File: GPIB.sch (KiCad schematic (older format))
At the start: 11 parts

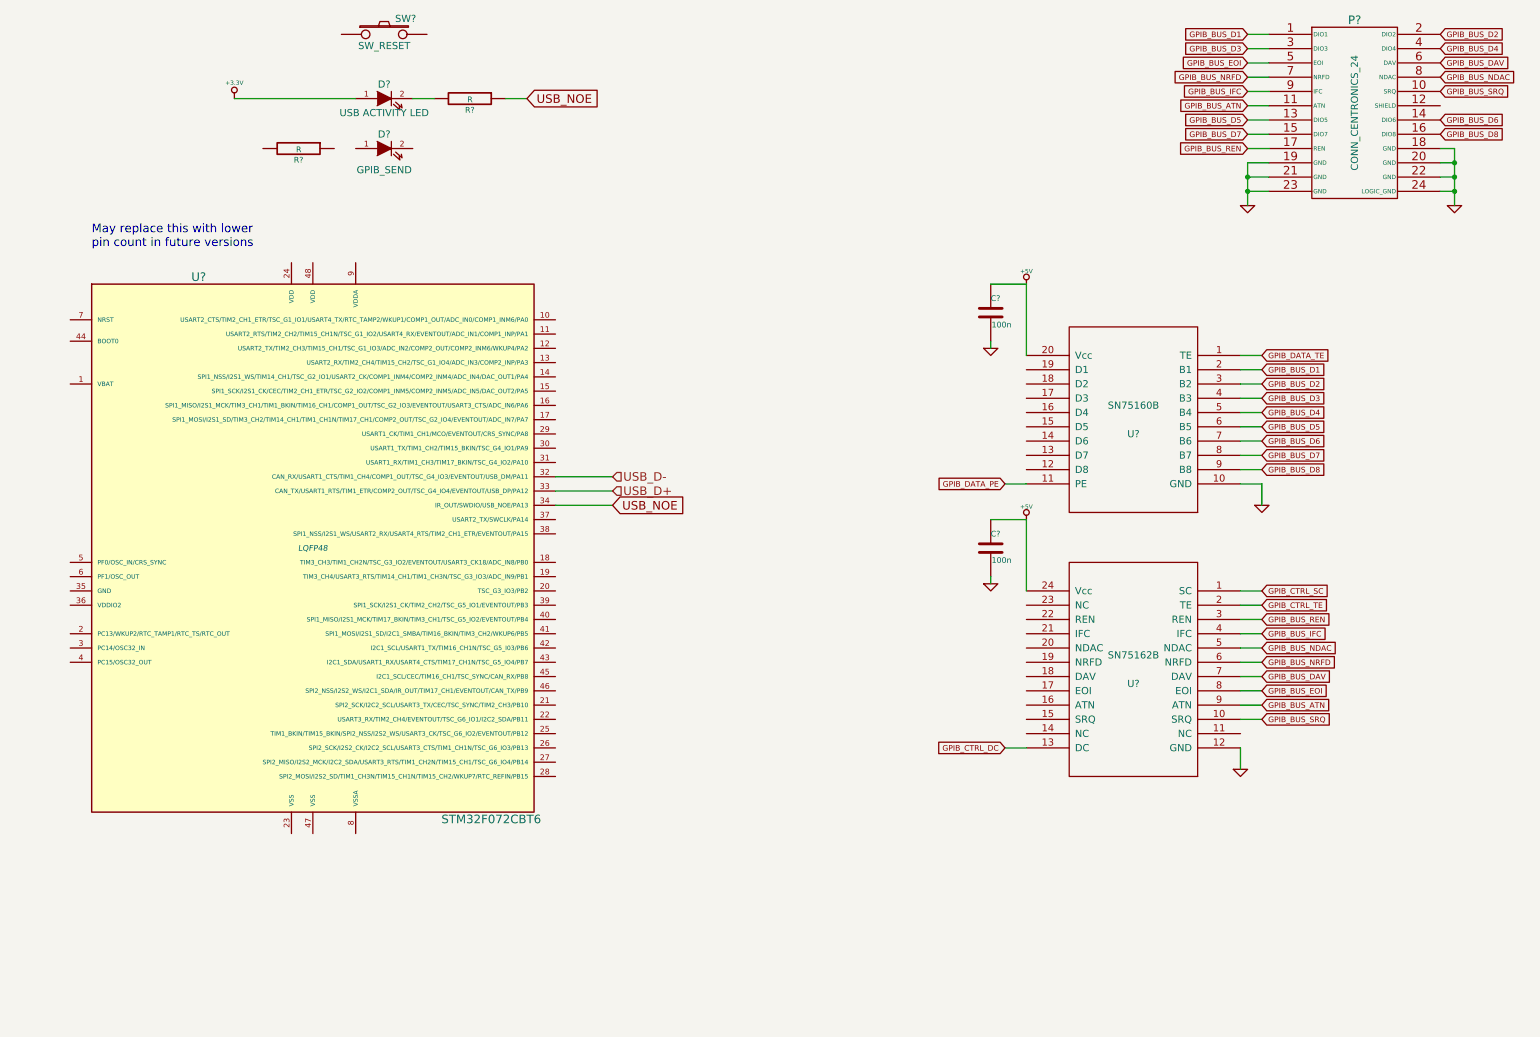
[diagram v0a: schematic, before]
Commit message: Add reset circuit
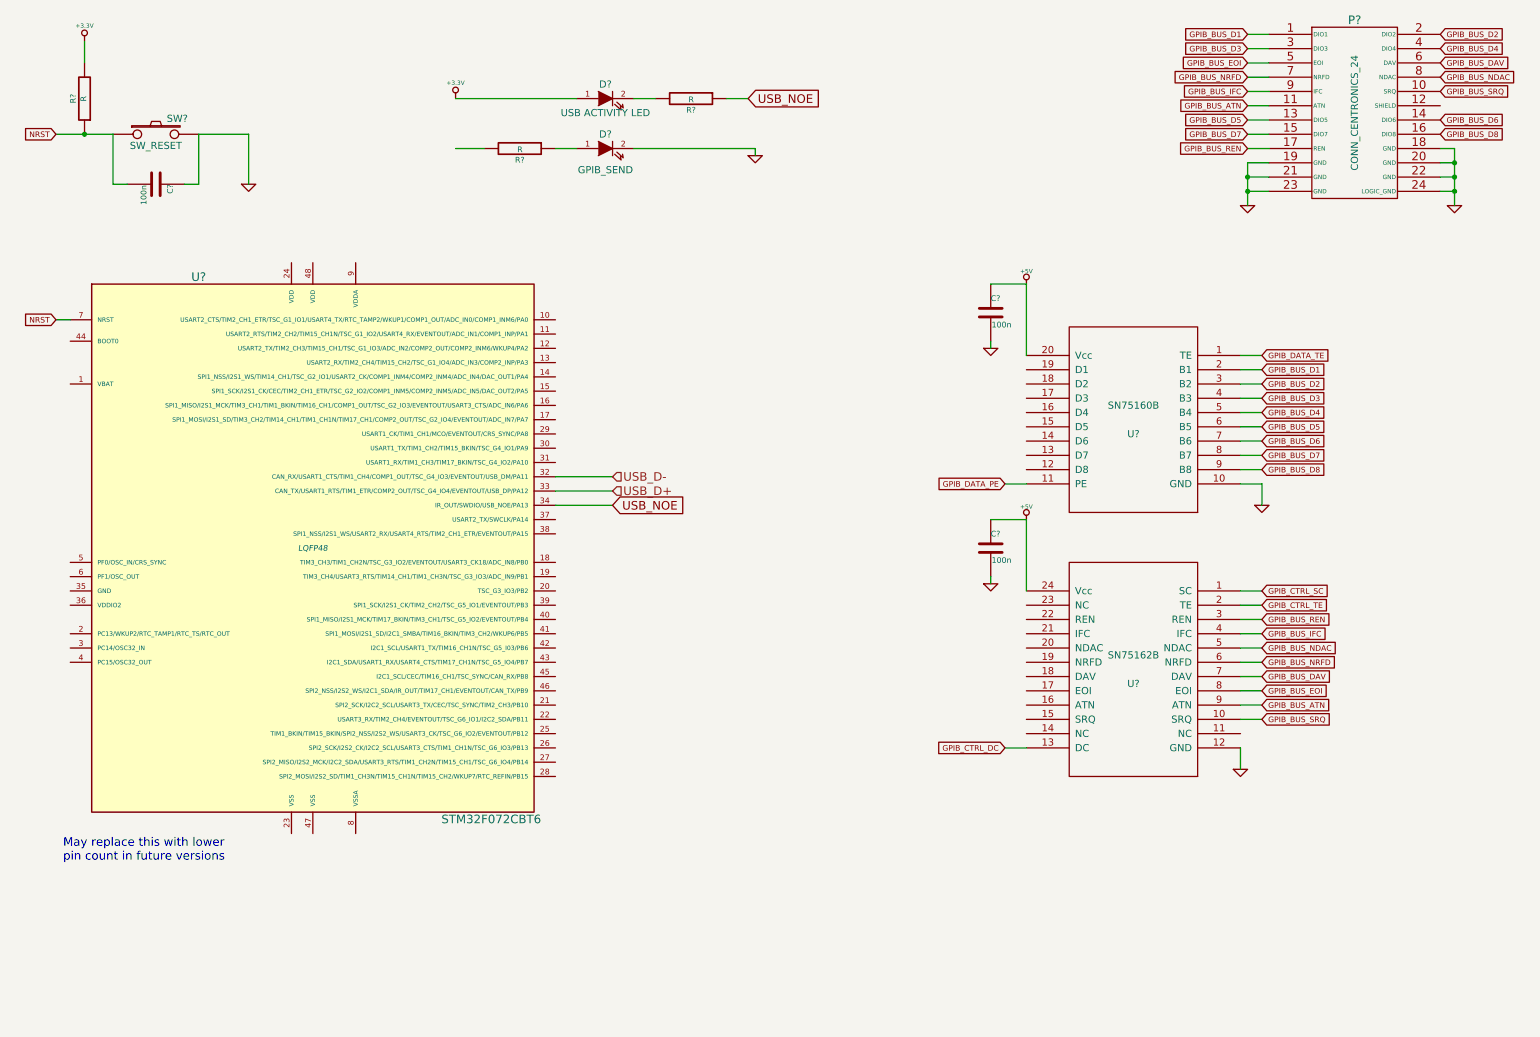
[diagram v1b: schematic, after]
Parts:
- added C?: 100n, symbol C
- added R?: R, symbol R
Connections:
- net +3.3V: now also R?.2
- net GND: now also D?.2 (K), SW?.2, C?.1
- net NRST: now reaches SW?.1
- net NRST: now also U?.7 (NRST), C?.2, R?.1
- net at D?.1 (A): now also R?.1
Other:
- moved on the sheet: D?, R?, SW?
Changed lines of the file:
@@
 L SW_PUSH SW?
 U 1 1 5566861E
-P 3250 750
-F 0 "SW?" H 3400 860 50  0000 C CNN
-F 1 "SW_RESET" H 3250 670 50  0000 C CNN
-F 2 "" H 3250 750 60  0000 C CNN
-F 3 "" H 3250 750 60  0000 C CNN
-	1    3250 750
+P 1650 1450
+F 0 "SW?" H 1800 1560 50  0000 C CNN
+F 1 "SW_RESET" H 1650 1370 50  0000 C CNN
+F 2 "" H 1650 1450 60  0000 C CNN
+F 3 "" H 1650 1450 60  0000 C CNN
+	1    1650 1450
 	1    0    0    -1
 $EndComp
@@
 L LED D?
 U 1 1 55668641
-P 3250 1550
-F 0 "D?" H 3250 1650 50  0000 C CNN
-F 1 "GPIB_SEND" H 3250 1400 50  0000 C CNN
-F 2 "" H 3250 1550 60  0000 C CNN
-F 3 "" H 3250 1550 60  0000 C CNN
-	1    3250 1550
-	1    0    0    -1
-$EndComp
-Text Notes 1200 2250 0    60   ~ 0
+P 4800 1550
+F 0 "D?" H 4800 1650 50  0000 C CNN
+F 1 "GPIB_SEND" H 4800 1400 50  0000 C CNN
+F 2 "" H 4800 1550 60  0000 C CNN
+F 3 "" H 4800 1550 60  0000 C CNN
+	1    4800 1550
+	1    0    0    -1
+$EndComp
+Text Notes 1000 6550 0    60   ~ 0
 May replace this with lower\npin count in future versions
 $Comp
@@
 L LED D?
 U 1 1 5567B154
-P 3250 1200
-F 0 "D?" H 3250 1300 50  0000 C CNN
-F 1 "USB ACTIVITY LED" H 3250 1100 50  0000 C CNN
-F 2 "" H 3250 1200 60  0000 C CNN
-F 3 "" H 3250 1200 60  0000 C CNN
-	1    3250 1200
+P 4800 1200
+F 0 "D?" H 4800 1300 50  0000 C CNN
+F 1 "USB ACTIVITY LED" H 4800 1100 50  0000 C CNN
+F 2 "" H 4800 1200 60  0000 C CNN
+F 3 "" H 4800 1200 60  0000 C CNN
+	1    4800 1200
 	1    0    0    -1
 $EndComp
@@
 L +3.3V #PWR?
 U 1 1 5567B18B
-P 2200 1200
-F 0 "#PWR?" H 2200 1160 30  0001 C CNN
-F 1 "+3.3V" H 2200 1310 30  0000 C CNN
-F 2 "" H 2200 1200 60  0000 C CNN
-F 3 "" H 2200 1200 60  0000 C CNN
-	1    2200 1200
-	1    0    0    -1
-$EndComp
-Wire Wire Line
-	2200 1200 3050 1200
+P 3750 1200
+F 0 "#PWR?" H 3750 1160 30  0001 C CNN
+F 1 "+3.3V" H 3750 1310 30  0000 C CNN
+F 2 "" H 3750 1200 60  0000 C CNN
+F 3 "" H 3750 1200 60  0000 C CNN
+	1    3750 1200
+	1    0    0    -1
+$EndComp
+Wire Wire Line
+	3750 1200 4600 1200
 $Comp
 L R R?
 U 1 1 5567B1D4
-P 3850 1200
-F 0 "R?" V 3930 1200 40  0000 C CNN
-F 1 "R" V 3857 1201 40  0000 C CNN
-F 2 "" V 3780 1200 30  0000 C CNN
-F 3 "" H 3850 1200 30  0000 C CNN
-	1    3850 1200
+P 5400 1200
+F 0 "R?" V 5480 1200 40  0000 C CNN
+F 1 "R" V 5407 1201 40  0000 C CNN
+F 2 "" V 5330 1200 30  0000 C CNN
+F 3 "" H 5400 1200 30  0000 C CNN
+	1    5400 1200
 	0    1    1    0
 $EndComp
 Wire Wire Line
-	3450 1200 3600 1200
-Wire Wire Line
-	4100 1200 4250 1200
+	5000 1200 5150 1200
+Wire Wire Line
+	5650 1200 5800 1200
 Text GLabel 4850 4050 2    60   Input ~ 0
 USB_NOE
-Text GLabel 4250 1200 2    60   Input ~ 0
+Text GLabel 5800 1200 2    60   Input ~ 0
 USB_NOE
 $Comp
 L R R?
 U 1 1 5567BB74
-P 2650 1550
-F 0 "R?" V 2730 1550 40  0000 C CNN
-F 1 "R" V 2657 1551 40  0000 C CNN
-F 2 "" V 2580 1550 30  0000 C CNN
-F 3 "" H 2650 1550 30  0000 C CNN
-	1    2650 1550
+P 4200 1550
+F 0 "R?" V 4280 1550 40  0000 C CNN
+F 1 "R" V 4207 1551 40  0000 C CNN
+F 2 "" V 4130 1550 30  0000 C CNN
+F 3 "" H 4200 1550 30  0000 C CNN
+	1    4200 1550
 	0    1    1    0
 $EndComp
@@
 Wire Wire Line
 	7500 4150 7750 4150
+$Comp
+L GND #PWR?
+U 1 1 5569A4CE
+P 5850 1600
+F 0 "#PWR?" H 5850 1600 30  0001 C CNN
+F 1 "GND" H 5850 1530 30  0001 C CNN
+F 2 "" H 5850 1600 60  0000 C CNN
+F 3 "" H 5850 1600 60  0000 C CNN
+	1    5850 1600
+	1    0    0    -1
+$EndComp
+Wire Wire Line
+	5000 1550 5850 1550
+Wire Wire Line
+	5850 1550 5850 1600
+Wire Wire Line
+	4600 1550 4450 1550
+Wire Wire Line
+	3950 1550 3750 1550
+$Comp
+L +3.3V #PWR?
+U 1 1 5569A6B6
+P 1150 800
+F 0 "#PWR?" H 1150 760 30  0001 C CNN
+F 1 "+3.3V" H 1150 910 30  0000 C CNN
+F 2 "" H 1150 800 60  0000 C CNN
+F 3 "" H 1150 800 60  0000 C CNN
+	1    1150 800
+	1    0    0    -1
+$EndComp
+$Comp
+L GND #PWR?
+U 1 1 5569A6D7
+P 2300 1800
+F 0 "#PWR?" H 2300 1800 30  0001 C CNN
+F 1 "GND" H 2300 1730 30  0001 C CNN
+F 2 "" H 2300 1800 60  0000 C CNN
+F 3 "" H 2300 1800 60  0000 C CNN
+	1    2300 1800
+	1    0    0    -1
+$EndComp
+$Comp
+L C C?
+U 1 1 5569A6F8
+P 1650 1800
+F 0 "C?" H 1650 1900 40  0000 L CNN
+F 1 "100n" H 1656 1715 40  0000 L CNN
+F 2 "" H 1688 1650 30  0000 C CNN
+F 3 "" H 1650 1800 60  0000 C CNN
+	1    1650 1800
+	0    1    1    0
+$EndComp
+$Comp
+L R R?
+U 1 1 5569A770
+P 1150 1200
+F 0 "R?" V 1230 1200 40  0000 C CNN
+F 1 "R" V 1157 1201 40  0000 C CNN
+F 2 "" V 1080 1200 30  0000 C CNN
+F 3 "" H 1150 1200 30  0000 C CNN
+	1    1150 1200
+	-1   0    0    1
+$EndComp
+Wire Wire Line
+	1150 800  1150 950
+Wire Wire Line
+	950  1450 1350 1450
+Connection ~ 1150 1450
+Wire Wire Line
+	1350 1450 1350 1800
+Wire Wire Line
+	1350 1800 1450 1800
+Wire Wire Line
+	1950 1450 1950 1800
+Wire Wire Line
+	1950 1800 1850 1800
+Wire Wire Line
+	1950 1450 2300 1450
+Wire Wire Line
+	2300 1450 2300 1800
+Wire Wire Line
+	1050 2750 950  2750
+Text GLabel 950  2750 0    39   Input ~ 0
+NRST
+Text GLabel 950  1450 0    39   Input ~ 0
+NRST
 $EndSCHEMATC

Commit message: initial GPIB pin mappings
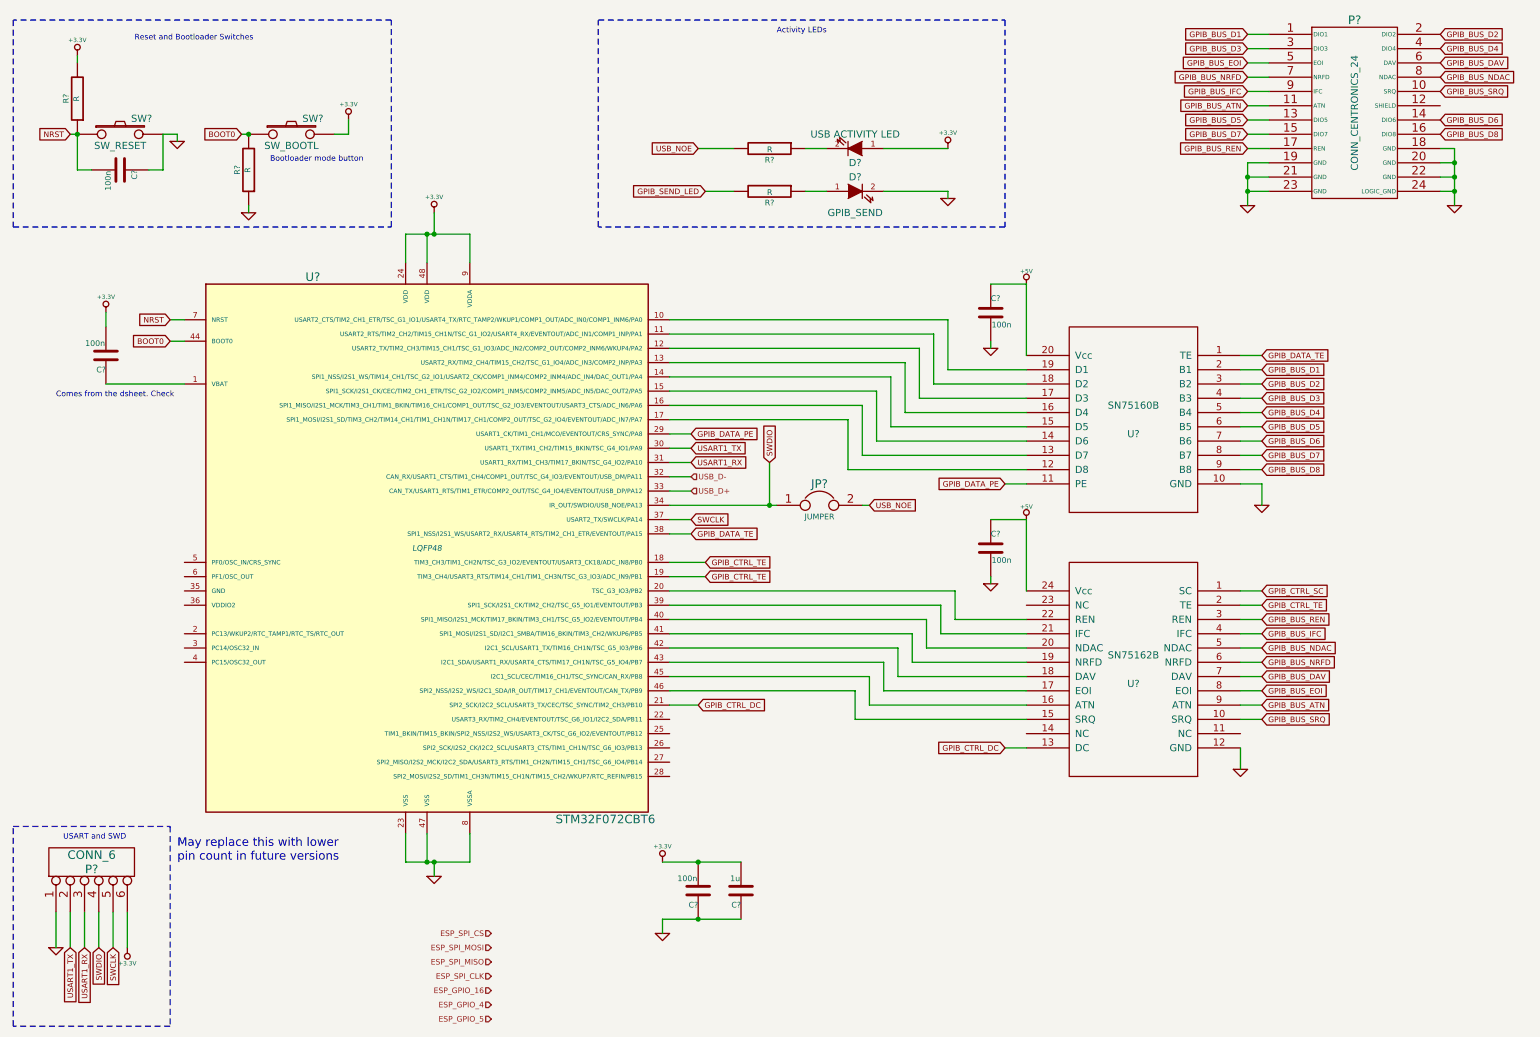
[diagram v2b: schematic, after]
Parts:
- added C? (x2): 100n, symbol C
- added C?: 1u, symbol C
- added JP?: JUMPER, symbol JUMPER
- added P?: CONN_6, symbol CONN_6
- added R?: R, symbol R
- added SW?: SW_BOOTL, symbol SW_PUSH
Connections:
- net +3.3V: now also U?.24 (VDD), U?.48 (VDD), U?.9 (VDDA), C?.2, C?.2, C?.2, P?.6, SW?.2
- net GND: now also U?.23 (VSS), U?.47 (VSS), U?.8 (VSSA), C?.1, C?.1, P?.1, R?.1
- net GPIB_CTRL_DC: now also U?.21 (SPI2_SCK/I2C2_SCL/USART3_TX/CEC/TSC_SYNC/TIM2_CH3/PB10)
- net GPIB_CTRL_TE: now also U?.18 (TIM3_CH3/TIM1_CH2N/TSC_G3_IO2/EVENTOUT/USART3_CK18/ADC_IN8/PB0), U?.19 (TIM3_CH4/USART3_RTS/TIM14_CH1/TIM1_CH3N/TSC_G3_IO3/ADC_IN9/PB1)
- net GPIB_DATA_PE: now also U?.29 (USART1_CK/TIM1_CH1/MCO/EVENTOUT/CRS_SYNC/PA8)
- net GPIB_DATA_TE: now also U?.38 (SPI1_NSS/I2S1_WS/USART2_RX/USART4_RTS/TIM2_CH1_ETR/EVENTOUT/PA15)
- net USB_NOE: now also R?.2, JP?.2; no longer R?.1, U?.34 (IR_OUT/SWDIO/USB_NOE/PA13)
- net at U?.12 (D8): now also U?.17 (SPI1_MOSI/I2S1_SD/TIM3_CH2/TIM14_CH1/TIM1_CH1N/TIM17_CH1/COMP2_OUT/TSC_G2_IO4/EVENTOUT/ADC_IN7/PA7)
- net at U?.13 (D7): now also U?.16 (SPI1_MISO/I2S1_MCK/TIM3_CH1/TIM1_BKIN/TIM16_CH1/COMP1_OUT/TSC_G2_IO3/EVENTOUT/USART3_CTS/ADC_IN6/PA6)
- net at U?.14 (D6): now also U?.15 (SPI1_SCK/I2S1_CK/CEC/TIM2_CH1_ETR/TSC_G2_IO2/COMP1_INM5/COMP2_INM5/ADC_IN5/DAC_OUT2/PA5)
- net at U?.15 (D5): now also U?.14 (SPI1_NSS/I2S1_WS/TIM14_CH1/TSC_G2_IO1/USART2_CK/COMP1_INM4/COMP2_INM4/ADC_IN4/DAC_OUT1/PA4)
- net at U?.16 (D4): now also U?.13 (USART2_RX/TIM2_CH4/TIM15_CH2/TSC_G1_IO4/ADC_IN3/COMP2_INP/PA3)
- net at U?.17 (D3): now also U?.12 (USART2_TX/TIM2_CH3/TIM15_CH1/TSC_G1_IO3/ADC_IN2/COMP2_OUT/COMP2_INM6/WKUP4/PA2)
- net at U?.18 (D2): now also U?.11 (USART2_RTS/TIM2_CH2/TIM15_CH1N/TSC_G1_IO2/USART4_RX/EVENTOUT/ADC_IN1/COMP1_INP/PA1)
- net at U?.19 (D1): now also U?.10 (USART2_CTS/TIM2_CH1_ETR/TSC_G1_IO1/USART4_TX/RTC_TAMP2/WKUP1/COMP1_OUT/ADC_IN0/COMP1_INM6/PA0)
- net at U?.15 (SRQ): now also U?.46 (SPI2_NSS/I2S2_WS/I2C1_SDA/IR_OUT/TIM17_CH1/EVENTOUT/CAN_TX/PB9)
- net at U?.16 (ATN): now also U?.45 (I2C1_SCL/CEC/TIM16_CH1/TSC_SYNC/CAN_RX/PB8)
- net at U?.17 (EOI): now also U?.43 (I2C1_SDA/USART1_RX/USART4_CTS/TIM17_CH1N/TSC_G5_IO4/PB7)
- net at U?.18 (DAV): now also U?.42 (I2C1_SCL/USART1_TX/TIM16_CH1N/TSC_G5_I03/PB6)
- net at U?.19 (NRFD): now also U?.41 (SPI1_MOSI/I2S1_SD/I2C1_SMBA/TIM16_BKIN/TIM3_CH2/WKUP6/PB5)
- net at U?.20 (NDAC): now also U?.40 (SPI1_MISO/I2S1_MCK/TIM17_BKIN/TIM3_CH1/TSC_G5_IO2/EVENTOUT/PB4)
- net at U?.21 (IFC): now also U?.39 (SPI1_SCK/I2S1_CK/TIM2_CH2/TSC_G5_IO1/EVENTOUT/PB3)
- net at U?.22 (REN): now also U?.20 (TSC_G3_IO3/PB2)
- net at U?.1 (VBAT): now also C?.1
- net USART1_TX: now reaches U?.30 (USART1_TX/TIM1_CH2/TIM15_BKIN/TSC_G4_IO1/PA9)
- net USART1_TX: now also P?.2
- net USART1_RX: now reaches U?.31 (USART1_RX/TIM1_CH3/TIM17_BKIN/TSC_G4_IO2/PA10)
- net USART1_RX: now also P?.3
- net SWCLK: now reaches U?.37 (USART2_TX/SWCLK/PA14)
- net SWCLK: now also P?.5
- net BOOT0: now reaches U?.44 (BOOT0)
- net BOOT0: now also R?.2, SW?.1
- net at D?.2 (K): now also R?.1; no longer R?.2
- net GPIB_SEND_LED: now reaches R?.2
- new net SWDIO: JP?.1, P?.4, U?.34 (IR_OUT/SWDIO/USB_NOE/PA13)
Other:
- note added: "Activity LEDs"
- note added: "Bootloader mode button"
- note added: "Comes from the dsheet. Check\n"
- note added: "Reset and Bootloader Switches"
- note added: "USART and SWD"
- moved on the sheet: C?, D?, R?, SW?, U?
